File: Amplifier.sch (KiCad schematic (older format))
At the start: 5 parts

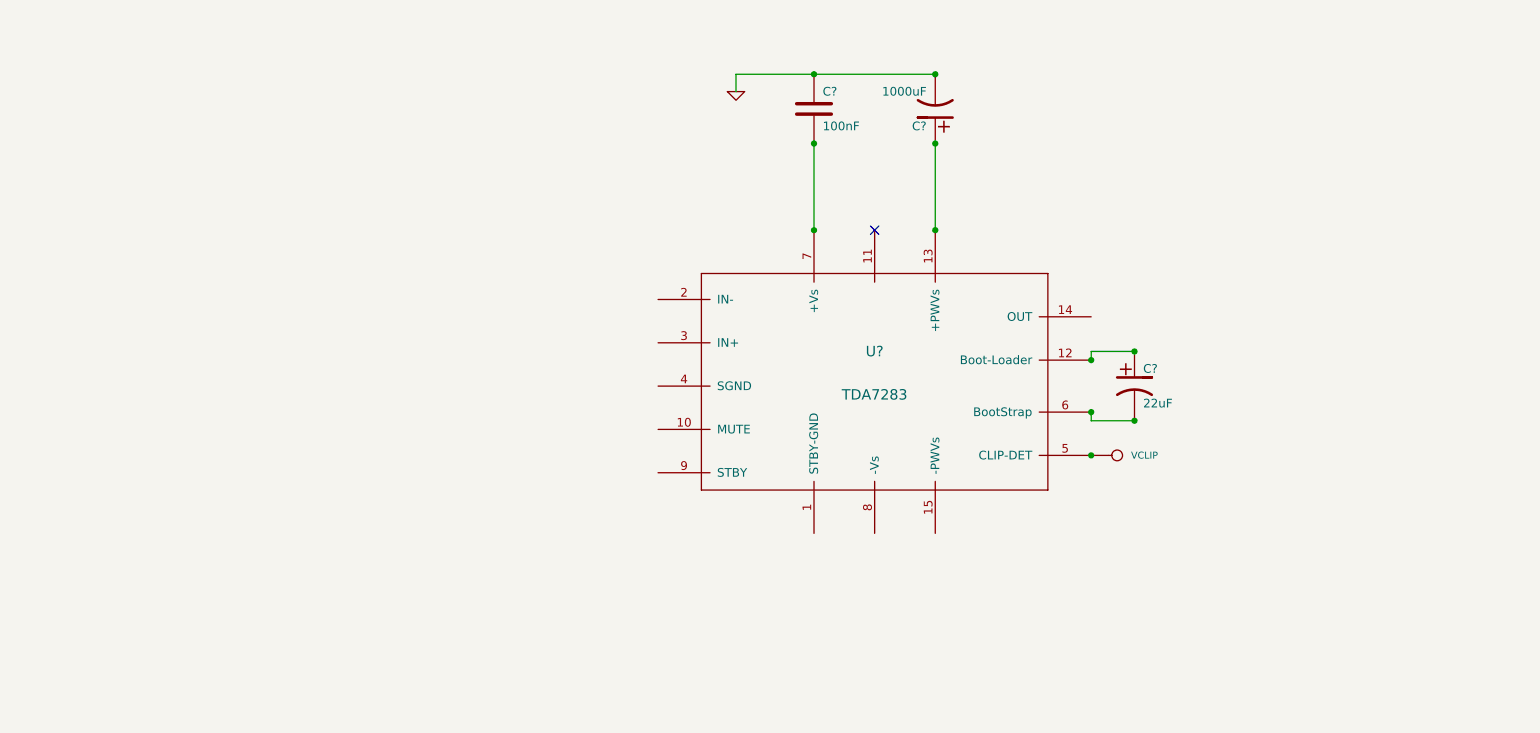
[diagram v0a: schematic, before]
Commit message: Added all components as shown in http://forum.diyefi.org/viewtopic.php?p=30734#p30734
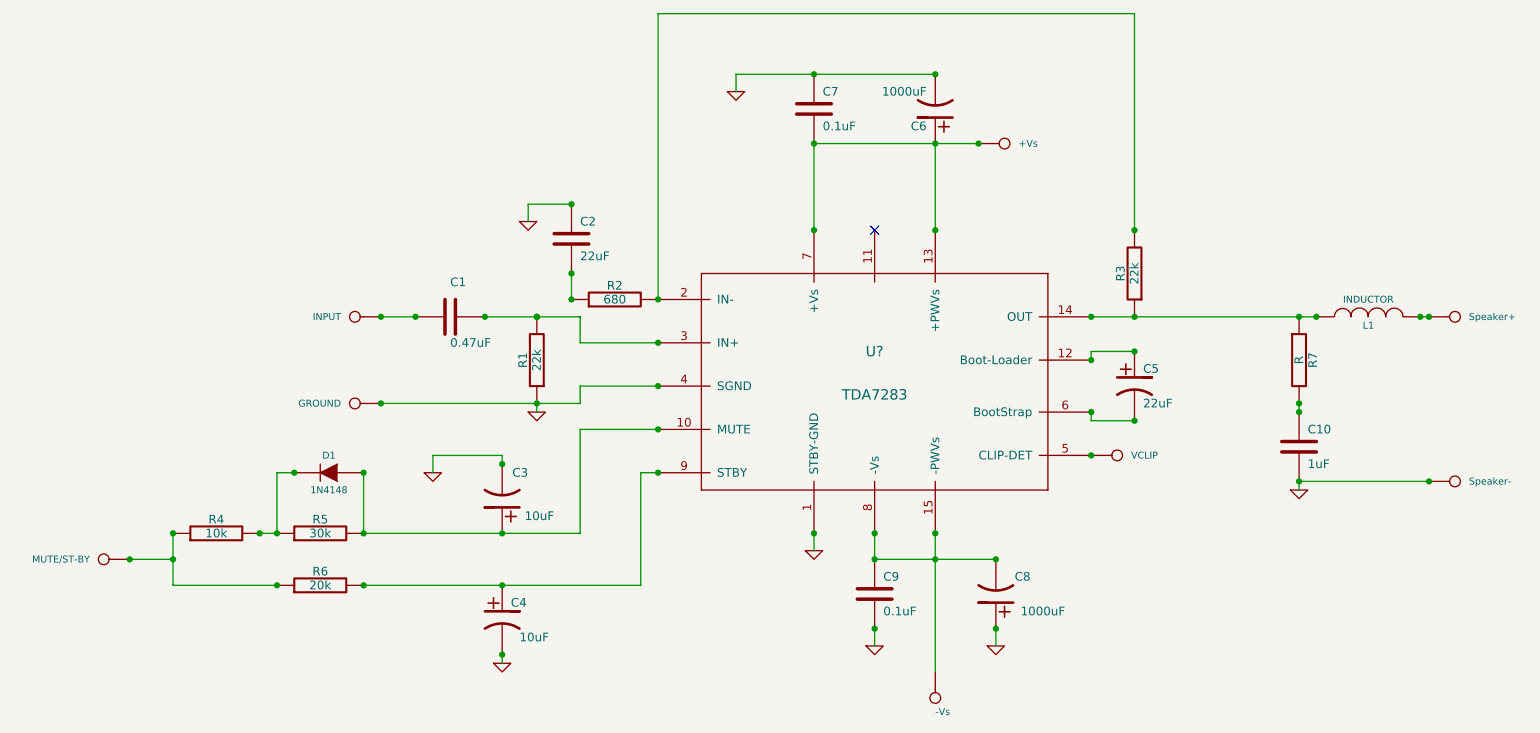
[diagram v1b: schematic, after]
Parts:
- added +Vs, -Vs, GROUND, INPUT, MUTE/ST-BY, Speaker+, Speaker-: CONN_1, symbol CONN_1
- added C1: 0.47uF, symbol C
- added C10: 1uF, symbol C
- added C2: 22uF, symbol C
- added C3, C4: 10uF, symbol CP1
- added C8: 1000uF, symbol CP1
- added C9: 0.1uF, symbol C
- added D1: 1N4148, symbol DIODE
- added L1: INDUCTOR, symbol INDUCTOR
- added R1, R3: 22k, symbol R
- added R2: 680, symbol R
- added R4: 10k, symbol R
- added R5: 30k, symbol R
- added R6: 20k, symbol R
- added R7: R, symbol R
- C7: renamed from C?; value 100nF -> 0.1uF
- gave numbers to parts that had none: 2
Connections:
- net GND: now also U?.1 (STBY-GND), U?.4 (SGND), C10.2, C2.1, C3.2 (-), C4.2 (-), C8.1 (+), C9.2, GROUND.1, R1.1, Speaker-.1
- net at U?.10 (MUTE): now also C3.1 (+), D1.1 (A), R5.2
- net at C6.1 (+), U?.13 (+PWVs): now also C7.2, U?.7 (+Vs), +Vs.1
- net at U?.14 (OUT): now also L1.1, R3.1, R7.1
- net at U?.15 (-PWVs): now also U?.8 (-Vs), -Vs.1, C8.2 (-), C9.1
- net at U?.2 (IN-): now also R2.2, R3.2
- net at U?.3 (IN+): now also C1.1, R1.2
- net at U?.9 (STBY): now also C4.1 (+), R6.2
- new net: L1.2, Speaker+.1
- new net: C2.2, R2.1
- new net: C1.2, INPUT.1
- new net: D1.2 (K), R4.2, R5.1
- new net: MUTE/ST-BY.1, R4.1, R6.1
- new net: C10.1, R7.2
